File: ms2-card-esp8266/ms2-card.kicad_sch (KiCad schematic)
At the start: 58 parts, among them J1 Schaltregler, J10 MicroSD_SPI_CD, J11 Conn_01x06, J2 ESP Prog, J20 Smartcard Connector, J21 PogoPin, J22 Card Edge, J23 Conn_01x04, J30 USB_B_Micro, J31 Power Select, J32 Conn_01x03, Q1 MMBT3904, Q2 MMBT3904, Q3 MMBT5401, SW1 RESET, U1 ESP-12F, U2 FM24C64B, U20 BL1551B, U3 BL1551B, U30 CP2102N-Axx-xQFN24, U4 BL1551B, U6 AMS1117-3.3

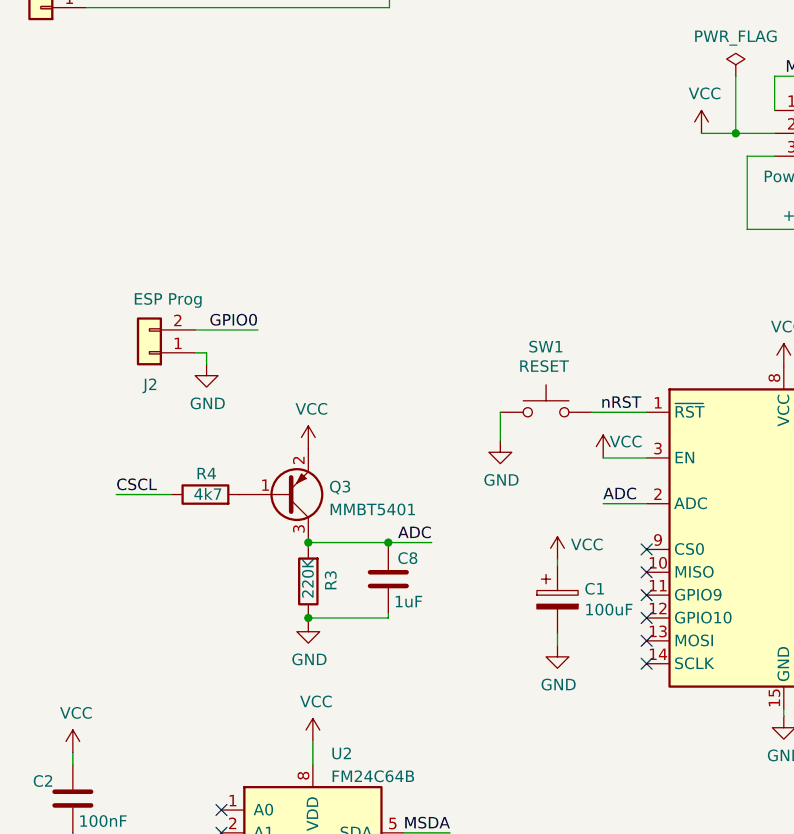
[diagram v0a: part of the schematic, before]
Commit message: add RC ADC oart
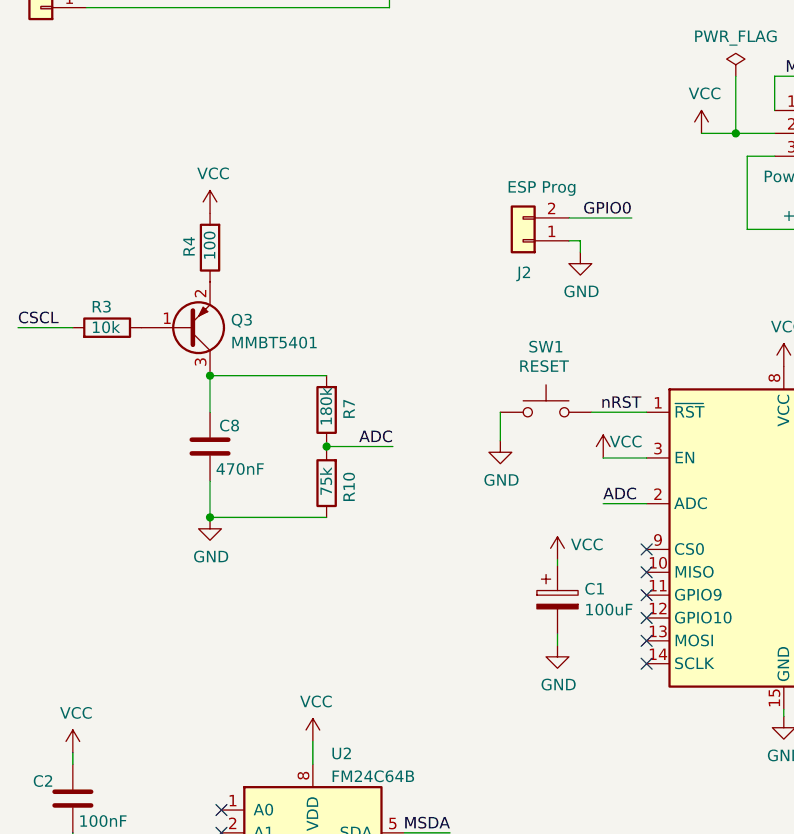
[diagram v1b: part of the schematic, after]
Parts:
- added R10: 75k, Resistor_SMD:R_0603_1608Metric, symbol Device:R
- added R3: 10k, Resistor_SMD:R_0603_1608Metric, symbol Device:R
- C8: value 1uF -> 470nF; LCSC C15849 -> C1623
- R4: value 4k7 -> 100; LCSC C23162 -> C22775
- R7: renamed from R3; value 220K -> 180k; LCSC C22961 -> C22827
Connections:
- net ADC: now also R7.1, R10.2; no longer C8.1, Q3.3 (C), R7.2
- net CSCL: now also R3.2; no longer R4.1
- net GND: now also R10.1; no longer R7.1
- net VCC: now also R4.2; no longer Q3.2 (E)
- net at Q3.1 (B): now also R3.1; no longer R4.2
- new net: C8.1, Q3.3 (C), R7.2
- new net: Q3.2 (E), R4.1
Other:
- moved on the sheet: C8, J2, Q3, R4, R7

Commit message: some small fixes
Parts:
- C1: now left out of the parts list
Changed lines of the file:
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@@
   (title_block
     (title "Lokkarten Emulator")
-    (date "2024-02-23")
-    (rev "0.97")
+    (date "2024-02-25")
+    (rev "0.98")
     (company "Modellbahn eXtreme")
     (comment 1 "Gerhard Bertelsmann")
@@
   )
   (symbol (lib_id "ms2-card-rescue:CP-Device") (at 76.708 118.872 0) (unit 1)
-    (in_bom yes) (on_board yes)
+    (in_bom no) (on_board yes)
     (property "Reference" "C1" (id 0) (at 79.7052 117.7036 0)
       (effects (font (size 1.27 1.27)) (justify left))

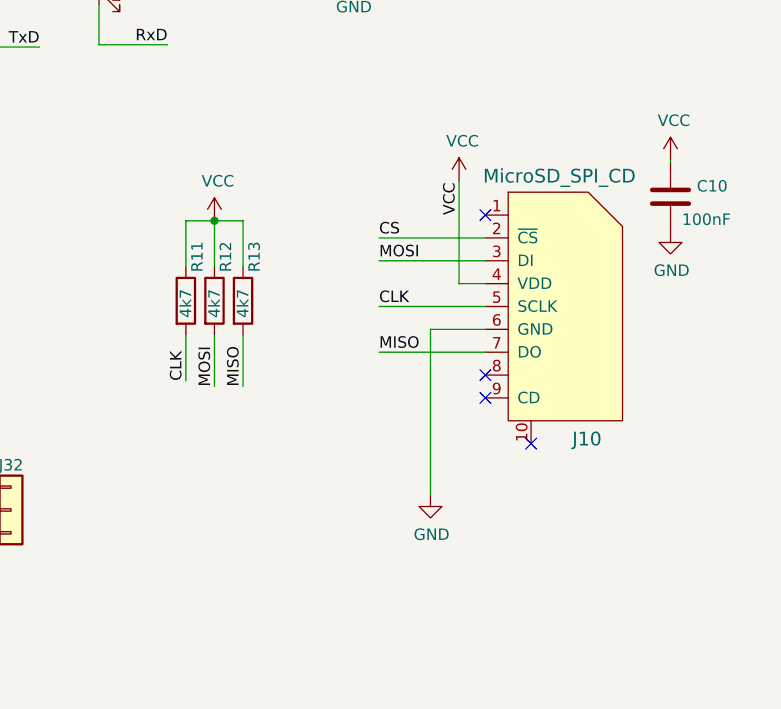
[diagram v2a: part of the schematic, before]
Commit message: pull up unused SD card IO pins
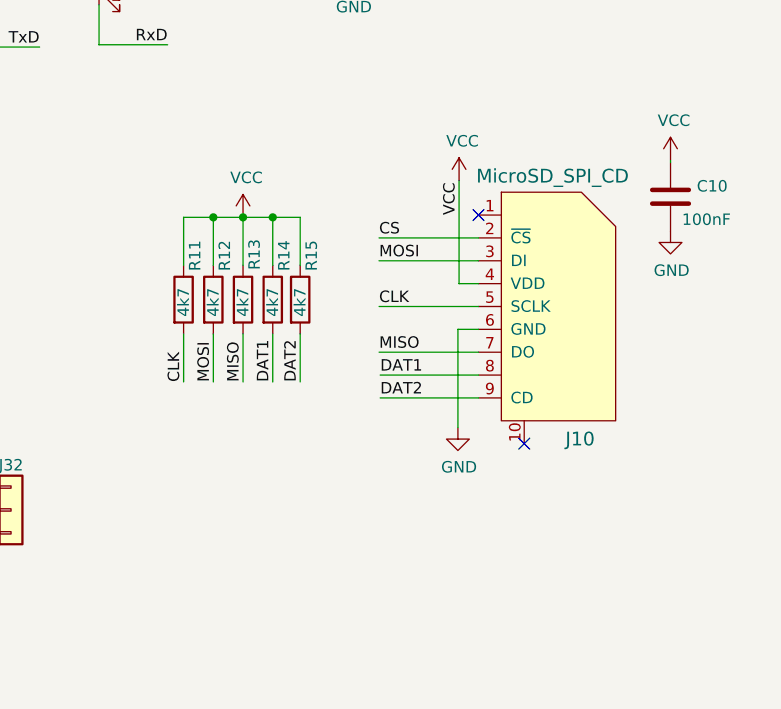
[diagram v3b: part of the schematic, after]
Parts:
- added R14, R15: 4k7, Resistor_SMD:R_0603_1608Metric, symbol Device:R
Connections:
- net VCC: now also R14.1, R15.1
- net DAT1: now reaches J10.8
- net DAT1: now also R14.2
- net DAT2: now reaches J10.9 (CD)
- net DAT2: now also R15.2
- no-connect marks 28 -> 26
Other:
- moved on the sheet: J10

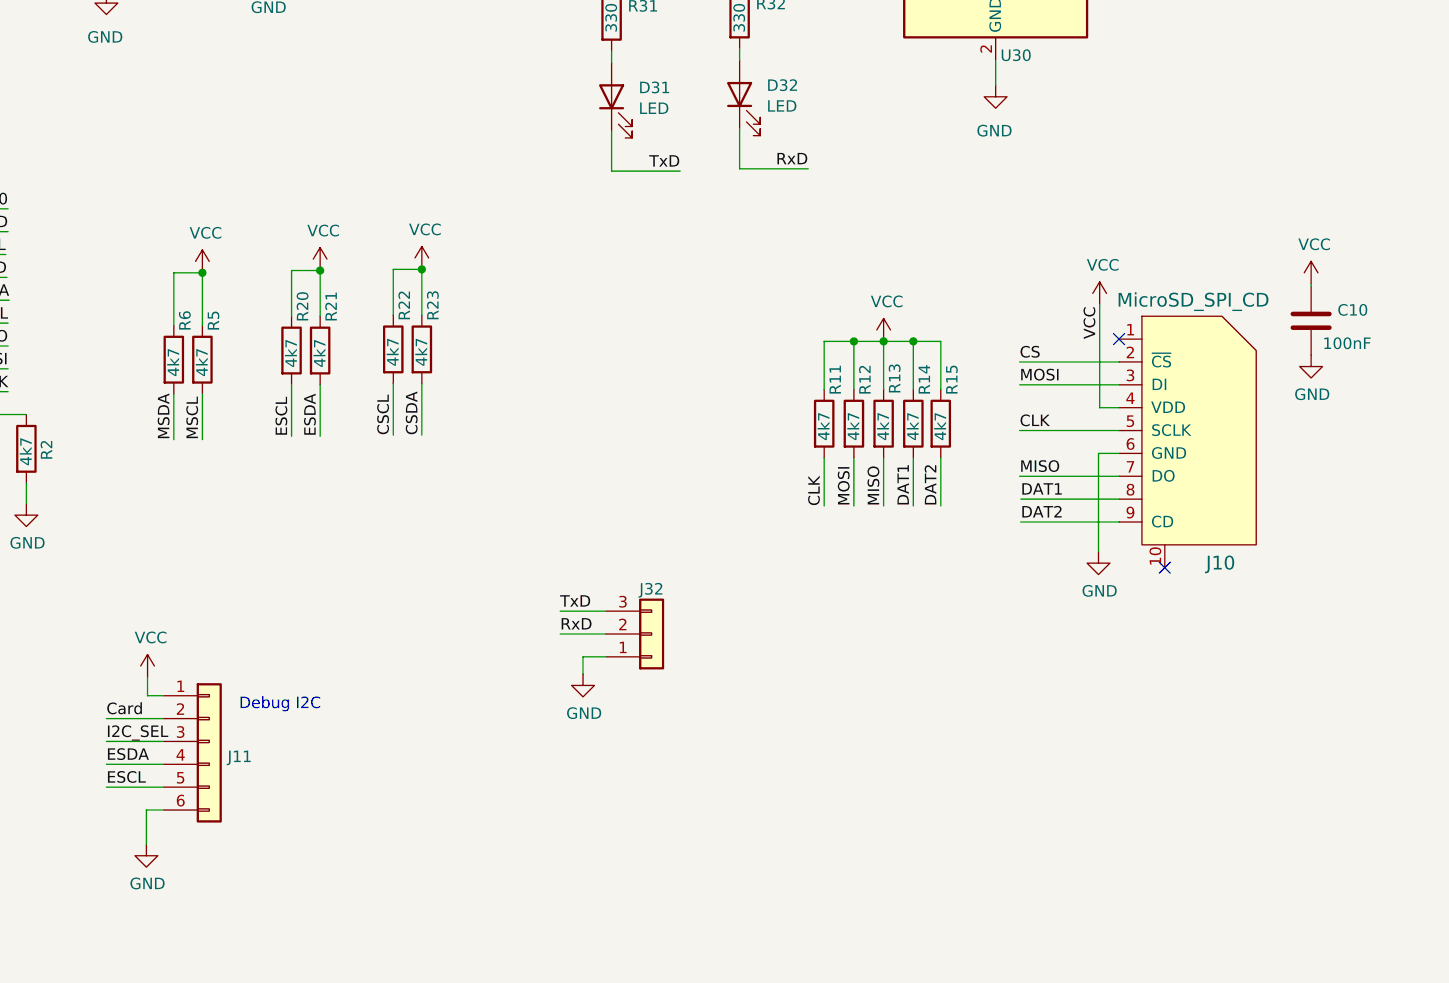
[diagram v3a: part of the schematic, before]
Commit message: add SPI EEPROM alternative
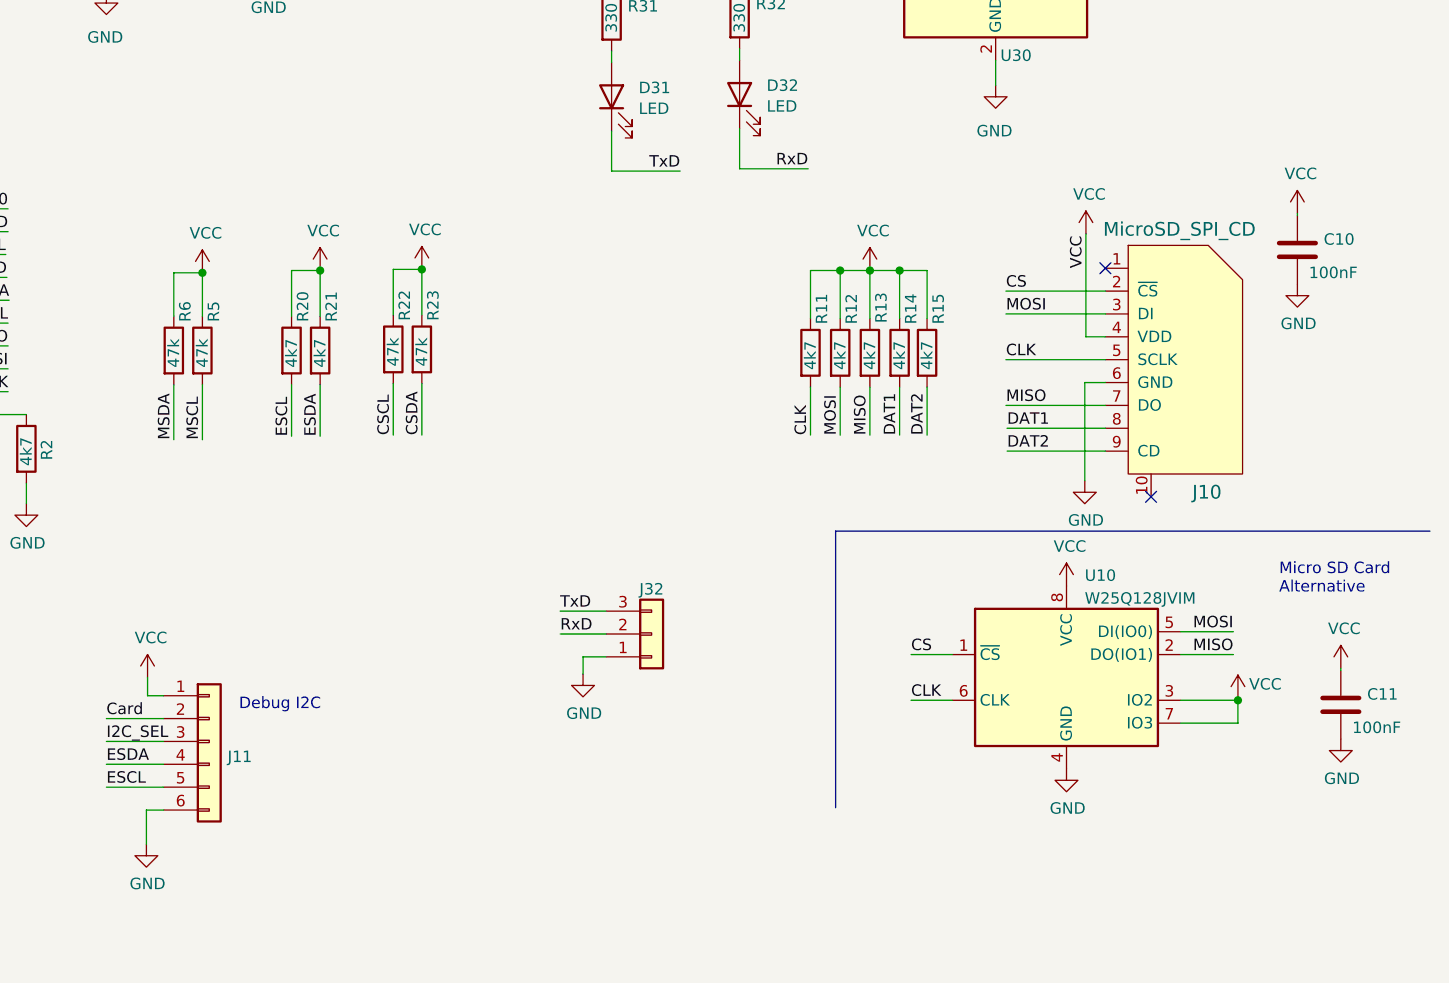
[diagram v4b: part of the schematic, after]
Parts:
- added C11: 100nF, Capacitor_SMD:C_0603_1608Metric, symbol Device:C
- added U10: W25Q128JVIM, Package_SO:SOIC-8_5.23x5.23mm_P1.27mm, symbol Memory_Flash:W25Q32JVSS
- J1, J11, J2, J20, J21, J22, J23, J31, J32, SW1: now left out of the parts list
- Q3: LCSC (none) -> C8326
- R22, R23, R5, R6: value 4k7 -> 47k; LCSC C23162 -> C25819
- U1: LCSC (none) -> C82891
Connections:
- net CLK: now also U10.6 (CLK)
- net CS: now also U10.1 (~{CS})
- net GND: now also C11.2, U10.4 (GND)
- net MISO: now also U10.2 (DO(IO1))
- net MOSI: now also U10.5 (DI(IO0))
- net VCC: now also C11.1, U10.3 (IO2), U10.7 (IO3), U10.8 (VCC)
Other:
- note added: "Micro SD Card Alternative"
- moved on the sheet: C10, J10, R11, R12, R13, R14, R15, R5, R6

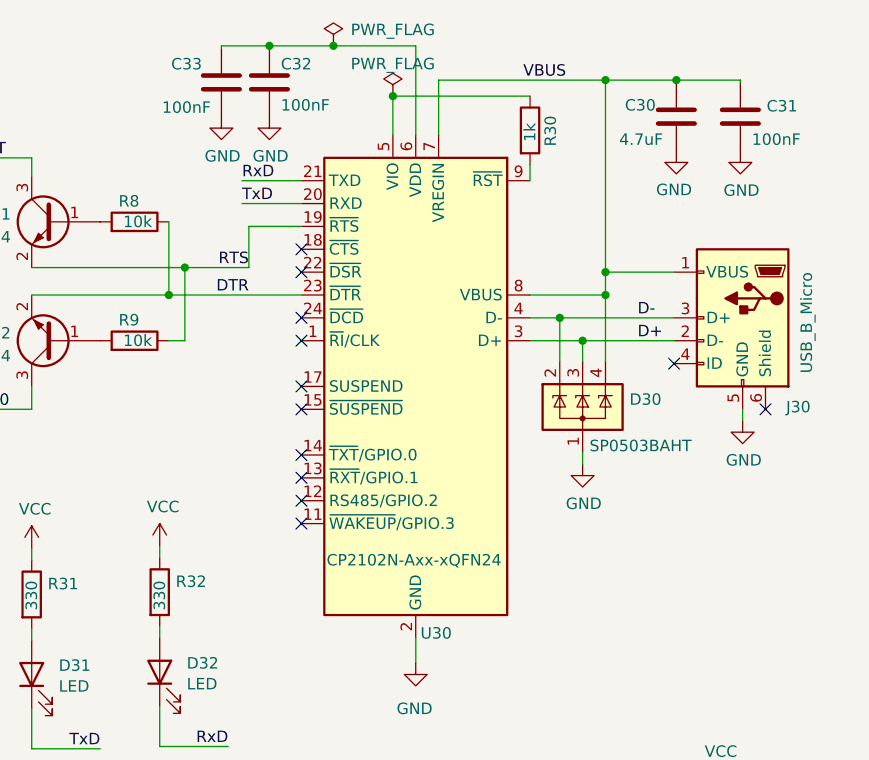
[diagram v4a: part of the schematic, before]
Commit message: small changes around CP2102
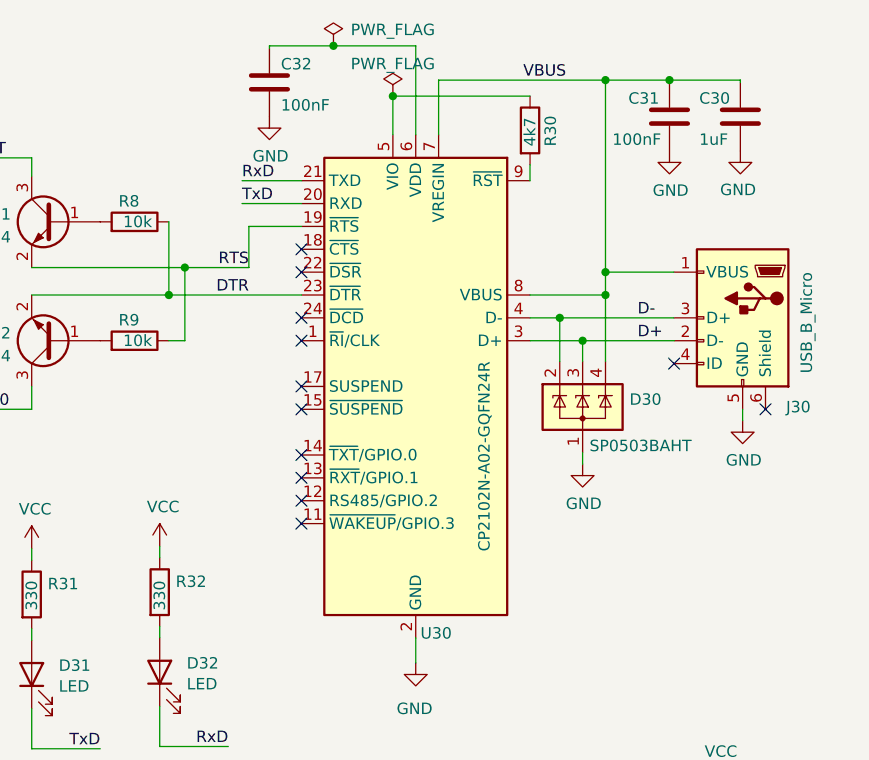
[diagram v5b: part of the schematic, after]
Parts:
- removed C33: 100nF, Capacitor_SMD:C_0603_1608Metric, symbol Device:C
- C30: value 4.7uF -> 1uF; LCSC C1779 -> C28323
- R30: value 1k -> 4k7; LCSC C21190 -> C23162
- U30: value CP2102N-Axx-xQFN24 -> CP2102N-A02-GQFN24R
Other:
- moved on the sheet: C30, C31

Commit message: add JLCPCB position fixes, except J10
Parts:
- D30, U2: JLCPCB Rotation Offset (none) -> -90
- J10, Q1, Q2, Q3, U20, U3, U4, U6: JLCPCB Rotation Offset (none) -> 180
- U1: JLCPCB Position Offset (none) -> 4.03,0.0; JLCPCB Rotation Offset (none) -> -90
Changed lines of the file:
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@@
+      (effects (font (size 1.27 1.27)) hide)
+    )
+    (property "JLCPCB Rotation Offset" "-90" (id 5) (at 49.53 147.32 0)
       (effects (font (size 1.27 1.27)) hide)
     )
@@
       (effects (font (size 1.27 1.27)) hide)
     )
+    (property "JLCPCB Rotation Offset" "180" (id 5) (at 102.87 173.99 0)
+      (effects (font (size 1.27 1.27)) hide)
+    )
     (pin "1")
     (pin "3")
@@
     )
     (property "LCSC" "C2944066" (id 4) (at 34.29 173.99 0)
+      (effects (font (size 1.27 1.27)) hide)
+    )
+    (property "JLCPCB Rotation Offset" "180" (id 5) (at 34.29 173.99 0)
       (effects (font (size 1.27 1.27)) hide)
     )
@@
     )
     (property "LCSC" "C82891" (id 4) (at 101.854 113.284 0)
+      (effects (font (size 1.27 1.27)) hide)
+    )
+    (property "JLCPCB Rotation Offset" "-90" (id 5) (at 101.854 113.284 0)
+      (effects (font (size 1.27 1.27)) hide)
+    )
+    (property "JLCPCB Position Offset" "4.03,0.0" (id 6) (at 101.854 113.284 0)
       (effects (font (size 1.27 1.27)) hide)
     )
@@
       (effects (font (size 1.27 1.27)) hide)
     )
+    (property "JLCPCB Rotation Offset" "180" (id 5) (at 52.07 176.53 0)
+      (effects (font (size 1.27 1.27)) hide)
+    )
     (pin "1")
     (pin "3")
@@
       (effects (font (size 1.27 1.27)) hide)
     )
+    (property "JLCPCB Rotation Offset" "-90" (id 5) (at 253.492 55.88 0)
+      (effects (font (size 1.27 1.27)) hide)
+    )
     (pin "1")
     (pin "2")
@@
       (effects (font (size 1.27 1.27)) hide)
     )
+    (property "JLCPCB Rotation Offset" "180" (id 5) (at 128.27 37.846 0)
+      (effects (font (size 1.27 1.27)) hide)
+    )
     (pin "1")
     (pin "3")
@@
       (effects (font (size 1.27 1.27)) hide)
     )
+    (property "JLCPCB Rotation Offset" "180" (id 5) (at 35.56 88.646 0)
+      (effects (font (size 1.27 1.27)) hide)
+    )
     (pin "1")
     (pin "2")
@@
     )
     (property "LCSC" "C20526" (id 4) (at 194.818 35.306 0)
+      (effects (font (size 1.27 1.27)) hide)
+    )
+    (property "JLCPCB Rotation Offset" "180" (id 5) (at 194.818 35.306 0)
       (effects (font (size 1.27 1.27)) hide)
     )
@@
       (effects (font (size 1.27 1.27)) hide)
     )
+    (property "JLCPCB Rotation Offset" "180" (id 5) (at 158.75 37.846 0)
+      (effects (font (size 1.27 1.27)) hide)
+    )
     (pin "1")
     (pin "3")
@@
       (effects (font (size 1.27 1.27)) hide)
     )
+    (property "JLCPCB Rotation Offset" "180" (id 5) (at 136.144 63.5 0)
+      (effects (font (size 1.27 1.27)) hide)
+    )
     (pin "1")
     (pin "2")
@@
       (effects (font (size 1.27 1.27)) hide)
     )
+    (property "JLCPCB Rotation Offset" "180" (id 5) (at 82.55 176.53 0)
+      (effects (font (size 1.27 1.27)) hide)
+    )
     (pin "1")
     (pin "3")
@@
     (property "LCSC" "C2889258" (id 4) (at 263.017 118.2352 0)
       (effects (font (size 1.27 1.27)) (justify right) hide)
+    )
+    (property "JLCPCB Rotation Offset" "180" (id 5) (at 256.032 114.808 0)
+      (effects (font (size 1.27 1.27)) hide)
+    )
+    (property "JLCPCB Position Offset" "" (id 6) (at 256.032 114.808 0)
+      (effects (font (size 1.27 1.27)) hide)
     )
     (pin "1")
@@
       (effects (font (size 1.27 1.27)) hide)
     )
+    (property "JLCPCB Rotation Offset" "180" (id 5) (at 194.818 48.514 0)
+      (effects (font (size 1.27 1.27)) hide)
+    )

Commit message: use latest 4.2 JLC production plugin to solve J10 paling issue
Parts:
- J10: JLCPCB Position Offset (none) -> 5.73,0.0
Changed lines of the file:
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@@
       (effects (font (size 1.27 1.27)) hide)
     )
-    (property "JLCPCB Position Offset" "" (id 6) (at 256.032 114.808 0)
+    (property "JLCPCB Position Offset" "5.73,0.0" (id 6) (at 256.032 114.808 0)
       (effects (font (size 1.27 1.27)) hide)
     )
